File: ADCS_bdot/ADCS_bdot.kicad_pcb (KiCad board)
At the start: 2 copper layers, 89.1 x 92.2 mm, 159 parts, among them IC1 STM32F411VCT6, J1 472192001, J5 2053380006, J6 5055671081, J7 2053380006, J8 MTLW-104-05-G-S-170-ND, T3 IRF7105TR, T4 IRF7105TR, U1 MCP2515-E/ML, U18 AMS1117-3.3, U19 A3G4250D, U2 TMCS1101A3BQDRQ1, U20 TMCS1101A3BQDRQ1, U22 SN65HVD230DR, U23 ADS1257IRGWT, U24 REF5025AID, U25 HMC1002-TR, U26 LM324NSR, U27 HMC1001-RC, U28 ADS1257IRGWT, U29 LM324NSR, U3 TMCS1101A3BQDRQ1, U30 DRV8833RTYR, U31 DRV8833RTYR, U4 TMCS1101A3BQDRQ1, U5 MT3608, U6 MT3608, Y1 ABLS-8.000MHZ-B2-T

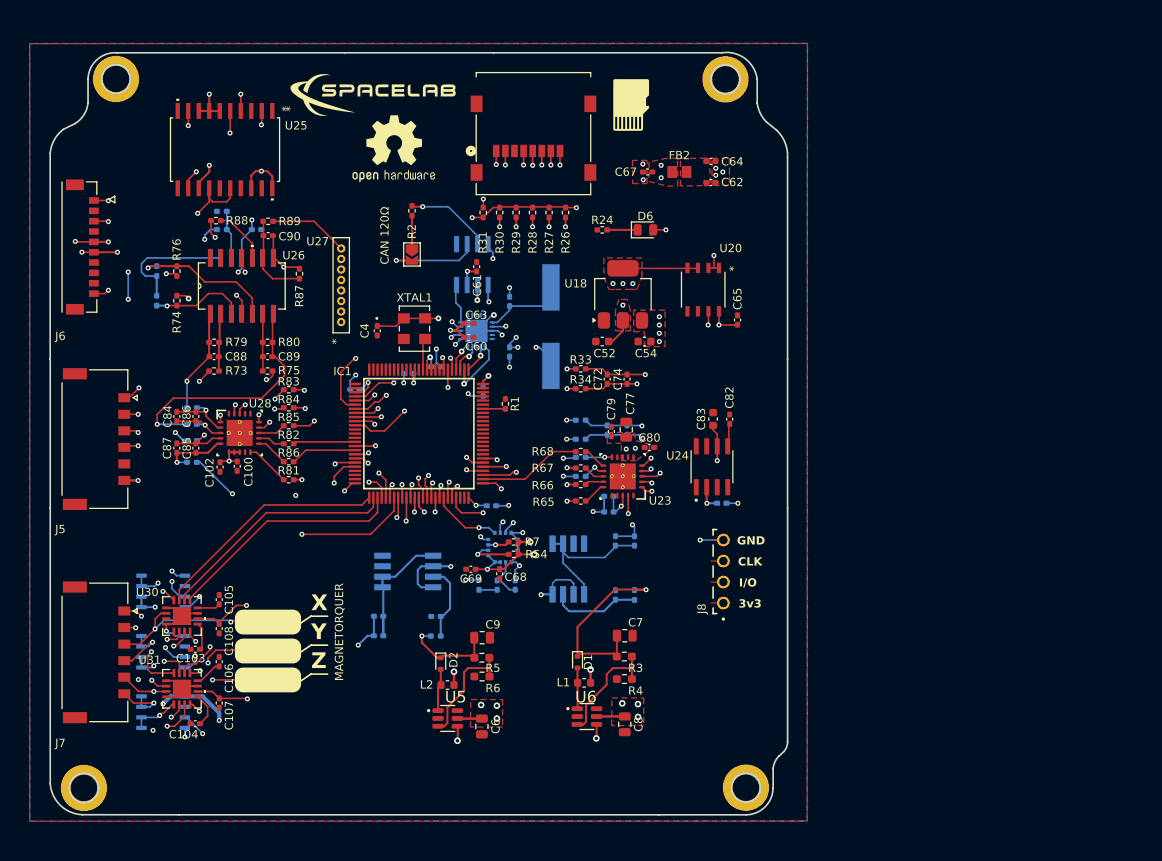
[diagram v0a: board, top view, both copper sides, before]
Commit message: add: schematic MCU Gyro Mag PWR
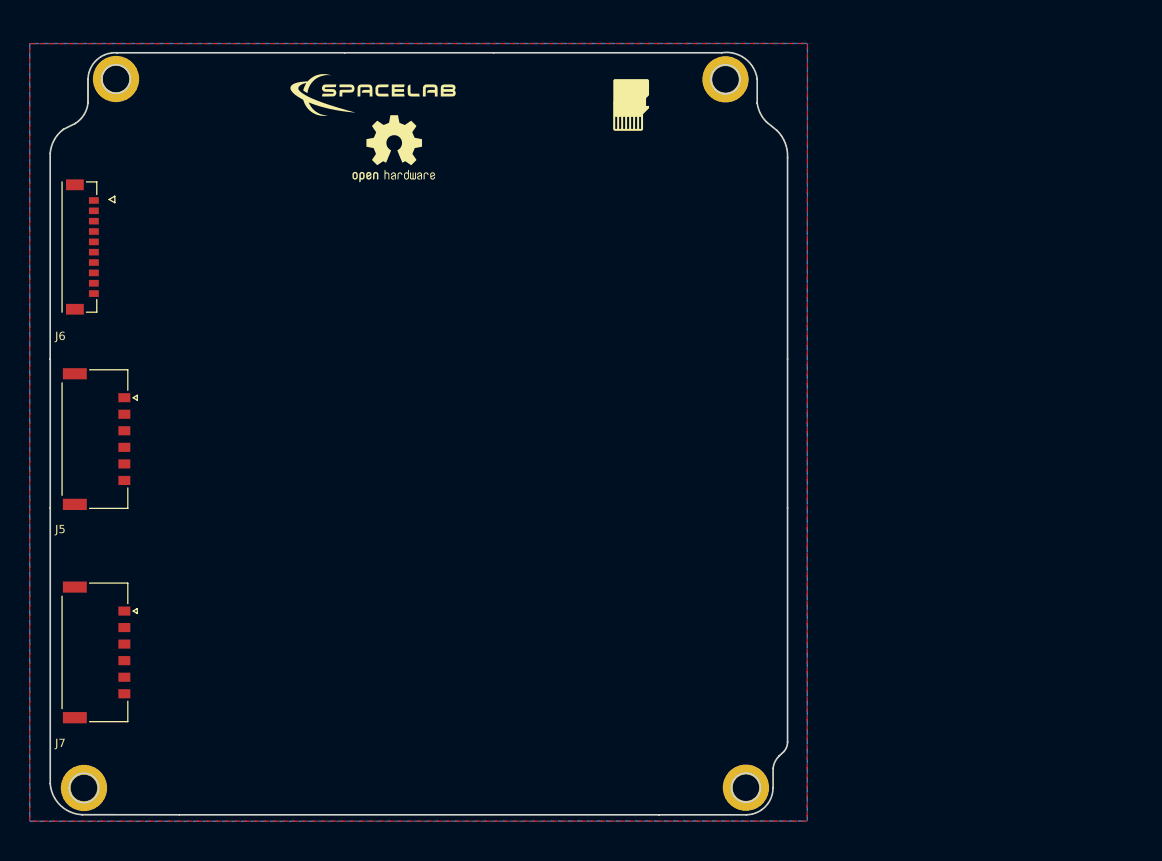
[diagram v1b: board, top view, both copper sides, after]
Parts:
- removed C1, C100, C5, C61, C63, C65, C98, C99: 100nF, Capacitor_SMD:C_0402_1005Metric_Pad0.74x0.62mm_HandSolder
- removed C101, C102, C107, C108, C60, C76, C95, C97: 10uF, Capacitor_SMD:C_0402_1005Metric_Pad0.74x0.62mm_HandSolder
- removed C103, C104, C62, C70: 10nF, Capacitor_SMD:C_0402_1005Metric_Pad0.74x0.62mm_HandSolder
- removed C105: 2.2uF, Capacitor_SMD:C_0402_1005Metric_Pad0.74x0.62mm_HandSolder
- removed C106: 2u2F, Capacitor_SMD:C_0402_1005Metric_Pad0.74x0.62mm_HandSolder
- removed C2, C3: 22pF, Capacitor_SMD:C_0402_1005Metric_Pad0.74x0.62mm_HandSolder
- removed C4: 0,01µF, Capacitor_SMD:C_0402_1005Metric_Pad0.74x0.62mm_HandSolder
- removed C52, C54, C83: 22uF, Capacitor_SMD:C_0603_1608Metric
- removed C6, C7, C8, C9: 22uF, Capacitor_SMD:C_0805_2012Metric
- removed C64, C67, C81, C82: 1uF, Capacitor_SMD:C_0402_1005Metric_Pad0.74x0.62mm_HandSolder
- removed C68: C0402C103K5RECAUTO, Capacitor_SMD:C_0402_1005Metric_Pad0.74x0.62mm_HandSolder
- removed C69: CL05B104KP5NNNC, Capacitor_SMD:C_0402_1005Metric_Pad0.74x0.62mm_HandSolder
- removed C71: 470nF, Capacitor_SMD:C_0402_1005Metric_Pad0.74x0.62mm_HandSolder
- removed C72, C73, C78, C79, C84, C85: 0.1uF, Capacitor_SMD:C_0402_1005Metric_Pad0.74x0.62mm_HandSolder
- removed C74, C75, C80, C86, C87: 100pF, Capacitor_SMD:C_0402_1005Metric_Pad0.74x0.62mm_HandSolder
- removed C77: 47uF, Capacitor_SMD:C_0805_2012Metric
- removed C88, C89, C90: 0.1µ1F, Capacitor_SMD:C_0402_1005Metric_Pad0.74x0.62mm_HandSolder
- removed C91, C92, C93, C94: 0.47uF, Capacitor_SMD:C_0402_1005Metric_Pad0.74x0.62mm_HandSolder
- removed C96: 0.1µF, Capacitor_SMD:C_0402_1005Metric_Pad0.74x0.62mm_HandSolder
- removed D1, D2: RB521S30T1G, Diode_SMD:D_SOD-523
- removed D10, D6, D8, D9: 150080GS75000, LED_SMD:LED_0805_2012Metric
- removed FB2: 2508051217Y6, adcs_board:IND_25_0805_FRT
- removed IC1: STM32F411VCT6, adcs_board:QFP50P1600X1600X160-100N
- removed J1: 472192001, adcs_board:CONN_47219-2001_MOL
- removed J8: MTLW-104-05-G-S-170-ND, adcs_board:SAMTEC_MTLW-104-X-X-S-X
- removed JP1: SolderJumper_2_Open, Jumper:SolderJumper-2_P1.3mm_Open_TrianglePad1.0x1.5mm
- removed L1, L2: 4.7uH, Inductor_SMD:L_0603_1608Metric
- removed R1, R24, R26, R27, R28, R29, R30, R31, R32: 10k, Resistor_SMD:R_0402_1005Metric_Pad0.72x0.64mm_HandSolder
- removed R2: 120, Resistor_SMD:R_0402_1005Metric_Pad0.72x0.64mm_HandSolder
- removed R3, R5: 7.5k, Resistor_SMD:R_0603_1608Metric_Pad0.98x0.95mm_HandSolder
- removed R33, R34, R35, R53, R69, R70, R71, R72: 301, Resistor_SMD:R_0402_1005Metric_Pad0.72x0.64mm_HandSolder
- removed R4, R6: 1k, Resistor_SMD:R_0603_1608Metric_Pad0.98x0.95mm_HandSolder
- removed R54, R7: 4,7k, Resistor_SMD:R_0402_1005Metric_Pad0.72x0.64mm_HandSolder
- removed R63, R64, R65, R66, R67, R68, R81, R82, R83, R84, R85, R86: 50, Resistor_SMD:R_0402_1005Metric_Pad0.72x0.64mm_HandSolder
- removed R73, R74, R75, R76, R79, R80, R87, R88, R89: 4.99k, Resistor_SMD:R_0402_1005Metric_Pad0.72x0.64mm_HandSolder
- removed R77, R78: 360k, Resistor_SMD:R_0402_1005Metric_Pad0.72x0.64mm_HandSolder
- removed R90, R92: 100, Resistor_SMD:R_0402_1005Metric_Pad0.72x0.64mm_HandSolder
- removed R91, R93: 1K, Resistor_SMD:R_0402_1005Metric_Pad0.72x0.64mm_HandSolder
- removed R94, R95, R96: 4k7, Resistor_SMD:R_0402_1005Metric_Pad0.72x0.64mm_HandSolder
- removed T3, T4: IRF7105TR, adcs_board:SO8
- removed U1: MCP2515-E/ML, adcs_board:QFN20_4x4MC_MCH-L
- removed U18: AMS1117-3.3, Package_TO_SOT_SMD:SOT-223-3_TabPin2
- removed U19: A3G4250D, adcs_board:LGA-16_4X4X1P1_STM-L
- removed U2, U20, U3, U4: TMCS1101A3BQDRQ1, adcs_board:SOIC8_D_TEX-L
- removed U22: SN65HVD230DR, adcs_board:SOIC127P599X175-8N
- removed U23, U28: ADS1257IRGWT, adcs_board:RGW0020A
- removed U24: REF5025AID, adcs_board:SOIC127P599X175-8N
- removed U25: HMC1002-TR, adcs_board:SOIC20_HNW
- removed U26, U29: LM324NSR, adcs_board:NS14
- removed U27: HMC1001-RC, adcs_board:SIP8_HMC1001_HNW
- removed U30, U31: DRV8833RTYR, adcs_board:RTY16
- removed U5, U6: MT3608, adcs_board:SOT95P280X145-6N
- removed XTAL1: ASFL1-100.000MHZ-L-T, adcs_board:ASFL1_ABR
- removed Y1: ABLS-8.000MHZ-B2-T, adcs_board:XTAL_ABLS-8.000MHZ-B2-T
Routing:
- net +3V3: track 83.9 -> 0.00 mm, vias 34 -> 0
- net GND: track 74.6 -> 0.00 mm, vias 23 -> 0
- net +5V: track 49.9 -> 0.00 mm, vias 20 -> 0
- net /magnetometer1/outy: track 30.2 -> 0.00 mm, vias 1 -> 0
- net /AIN1u7: track 29.0 -> 0.00 mm
- net /AIN2u7: track 29.0 -> 0.00 mm
- net /nsleepu7: track 28.8 -> 0.00 mm
- net /magnetometer1/8v(2): track 22.7 -> 0.00 mm, vias 1 -> 0
- net /magnetorquerx2: track 19.5 -> 0.00 mm, vias 2 -> 0
- net GNDA: track 19.1 -> 0.00 mm, vias 11 -> 0
- net Net-(C93-Pad2): track 19.0 -> 0.00 mm
- net /mcu_circuits/can_n: track 18.0 -> 0.00 mm, vias 4 -> 0
- net Net-(U26-2IN+): track 17.3 -> 0.00 mm, vias 1 -> 0
- net /nsleepu8: track 17.1 -> 0.00 mm, vias 2 -> 0
- net /magnetometer1/S/R2: track 16.9 -> 0.00 mm, vias 4 -> 0
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- removed copper zone on F.Cu, net +3.3VA
- removed copper zone on F.Cu, net +3V3
- removed copper zone on F.Cu, net +5V
- removed copper zone on F.Cu, net /mcu_circuits/5v_out
- removed copper zone on F.Cu, net GNDA
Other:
- board text removed: "*"
- board text removed: "3v3"
- board text removed: "CAN 120Ω"
- board text removed: "CLK"
- board text removed: "GND"
- board text removed: "I/O"
- board text removed: "MAGNETORQUER"
- board text removed: "X"
- board text removed: "Y"
- board text removed: "Z"

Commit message: add: a bunch of stuff
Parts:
- added C1: 100n, Capacitor_SMD:C_0603_1608Metric_Pad1.08x0.95mm_HandSolder, F.Cu at (221.2, 85.7)
- added C10: 10u, Capacitor_SMD:C_0603_1608Metric_Pad1.08x0.95mm_HandSolder, F.Cu at (131.8, 97.2)
- added C11: 100n, Capacitor_SMD:C_0603_1608Metric_Pad1.08x0.95mm_HandSolder, F.Cu at (143.8, 84.3)
- added C12: 100n, Capacitor_SMD:C_0603_1608Metric_Pad1.08x0.95mm_HandSolder, F.Cu at (148.8, 84.3)
- added C13: 100n, Capacitor_SMD:C_0603_1608Metric_Pad1.08x0.95mm_HandSolder, F.Cu at (158.8, 96.3)
- added C14: 100n, Capacitor_SMD:C_0603_1608Metric_Pad1.08x0.95mm_HandSolder, F.Cu at (158.8, 102.3)
- added C15: 100n, Capacitor_SMD:C_0603_1608Metric_Pad1.08x0.95mm_HandSolder, F.Cu at (134.8, 84.3)
- added C17: 10u, Capacitor_SMD:C_0603_1608Metric_Pad1.08x0.95mm_HandSolder, F.Cu at (157.8, 84.3)
- added C18: 10u, Capacitor_SMD:C_0603_1608Metric_Pad1.08x0.95mm_HandSolder, F.Cu at (131.8, 110.3)
- added C2: 2u2, Capacitor_SMD:C_0603_1608Metric_Pad1.08x0.95mm_HandSolder, F.Cu at (149.8, 113.3)
- added C21: 15p, Capacitor_SMD:C_0603_1608Metric_Pad1.08x0.95mm_HandSolder, F.Cu at (123.1, 98.2)
- added C22: 15p, Capacitor_SMD:C_0603_1608Metric_Pad1.08x0.95mm_HandSolder, F.Cu at (123.1, 102.1)
- added C23: 10p, Capacitor_SMD:C_0603_1608Metric_Pad1.08x0.95mm_HandSolder, F.Cu at (126.8, 90.3)
- added C24: 10p, Capacitor_SMD:C_0603_1608Metric_Pad1.08x0.95mm_HandSolder, F.Cu at (126.8, 94.3)
- added C25: 1u, Capacitor_SMD:C_0603_1608Metric_Pad1.08x0.95mm_HandSolder, F.Cu at (151.0, 72.0)
- added C26: 100n, Capacitor_SMD:C_0603_1608Metric_Pad1.08x0.95mm_HandSolder, F.Cu at (149.2, 72.0)
- added C27: 100n, Capacitor_SMD:C_0603_1608Metric_Pad1.08x0.95mm_HandSolder, F.Cu at (146.5, 69.4)
- added C28: 100n, Capacitor_SMD:C_0603_1608Metric_Pad1.08x0.95mm_HandSolder, F.Cu at (147.1, 74.6)
- added C29: 100n, Capacitor_SMD:C_0603_1608Metric_Pad1.08x0.95mm_HandSolder, F.Cu at (165.9, 68.2)
- added C3: 2u2, Capacitor_SMD:C_0603_1608Metric_Pad1.08x0.95mm_HandSolder, F.Cu at (158.8, 89.3)
- added C30: 1u, Capacitor_SMD:C_0603_1608Metric_Pad1.08x0.95mm_HandSolder, F.Cu at (165.9, 66.4)
- added C31: 100n, Capacitor_SMD:C_0603_1608Metric_Pad1.08x0.95mm_HandSolder, F.Cu at (169.8, 66.4)
- added C32: 100n, Capacitor_SMD:C_0603_1608Metric_Pad1.08x0.95mm_HandSolder, F.Cu at (169.8, 68.2)
- added C4: 100n, Capacitor_SMD:C_0603_1608Metric_Pad1.08x0.95mm_HandSolder, F.Cu at (136.8, 111.3)
- added C5: 100n, Capacitor_SMD:C_0603_1608Metric_Pad1.08x0.95mm_HandSolder, F.Cu at (143.8, 111.3)
- added C6: 100n, Capacitor_SMD:C_0603_1608Metric_Pad1.08x0.95mm_HandSolder, F.Cu at (149.8, 111.3)
- added C7: 100n, Capacitor_SMD:C_0603_1608Metric_Pad1.08x0.95mm_HandSolder, F.Cu at (158.8, 106.2)
- added C8: 22u, Capacitor_SMD:C_0603_1608Metric_Pad1.08x0.95mm_HandSolder, F.Cu at (170.9, 121.4)
- added C9: 100n, Capacitor_SMD:C_0603_1608Metric_Pad1.08x0.95mm_HandSolder, F.Cu at (131.8, 105.1)
- added IC1: STM32F746ZGT6, Footprintlib_adcs_bdot:QFP50P2200X2200X160-144N, F.Cu at (145.4, 97.8)
- added IC2: IIS2MDCTR, Footprintlib_adcs_bdot:IIS2MDCTR, F.Cu at (146.4, 72.0)
- added R1: 10k, Resistor_SMD:R_0603_1608Metric_Pad0.98x0.95mm_HandSolder, F.Cu at (226.0, 86.2)
- added R2: 0R, Resistor_SMD:R_0603_1608Metric_Pad0.98x0.95mm_HandSolder, F.Cu at (131.8, 101.3)
- added R3: 10k, Resistor_SMD:R_0603_1608Metric_Pad0.98x0.95mm_HandSolder, F.Cu at (159.0, 124.8)
- added R4: 10k, Resistor_SMD:R_0603_1608Metric_Pad0.98x0.95mm_HandSolder, F.Cu at (159.0, 127.3)
- added R5: 10R, Resistor_SMD:R_0603_1608Metric_Pad0.98x0.95mm_HandSolder, F.Cu at (152.8, 70.2)
- added R6: 10R, Resistor_SMD:R_0603_1608Metric_Pad0.98x0.95mm_HandSolder, F.Cu at (163.1, 69.9)
- added R7: 10R, Resistor_SMD:R_0603_1608Metric_Pad0.98x0.95mm_HandSolder, F.Cu at (172.4, 69.2)
- added R8: 261k, Resistor_SMD:R_0603_1608Metric_Pad0.98x0.95mm_HandSolder, F.Cu at (170.9, 123.9)
- added R9: 100k, Resistor_SMD:R_0603_1608Metric_Pad0.98x0.95mm_HandSolder, F.Cu at (170.9, 126.4)
- added U1: I3G4250DTR, Footprintlib_adcs_bdot:LGA-16_4X4X1_STM-M, F.Cu at (167.1, 71.8)
- added U3: TPSM861253RDXR, Footprintlib_adcs_bdot:RDX0007A-MFG, F.Cu at (153.1, 126.2)
- added Y1: ABM3-8.000MHZ-B4Y-T, Footprintlib_adcs_bdot:ABM3, F.Cu at (127.8, 100.3)
- added Y2: CM7V-T1A-32.768kHz-7pF-10PPM-TA-QC T3, Footprintlib_adcs_bdot:CM7V32768TBQA020, F.Cu at (130.8, 92.3)
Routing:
- net GND: vias 0 -> 2
- added copper zone on B.Cu, net (none)
- added copper zone on In1.Cu, net GND
- added copper zone on In2.Cu, net GND
- removed copper zone on B.Cu, net GNDA
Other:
- copper layers 2 -> 4
